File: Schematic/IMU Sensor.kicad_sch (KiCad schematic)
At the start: 17 parts, among them J31 IMU_nRESET, J32 IMU_INT, U25 BNO086, Y1 32.768k

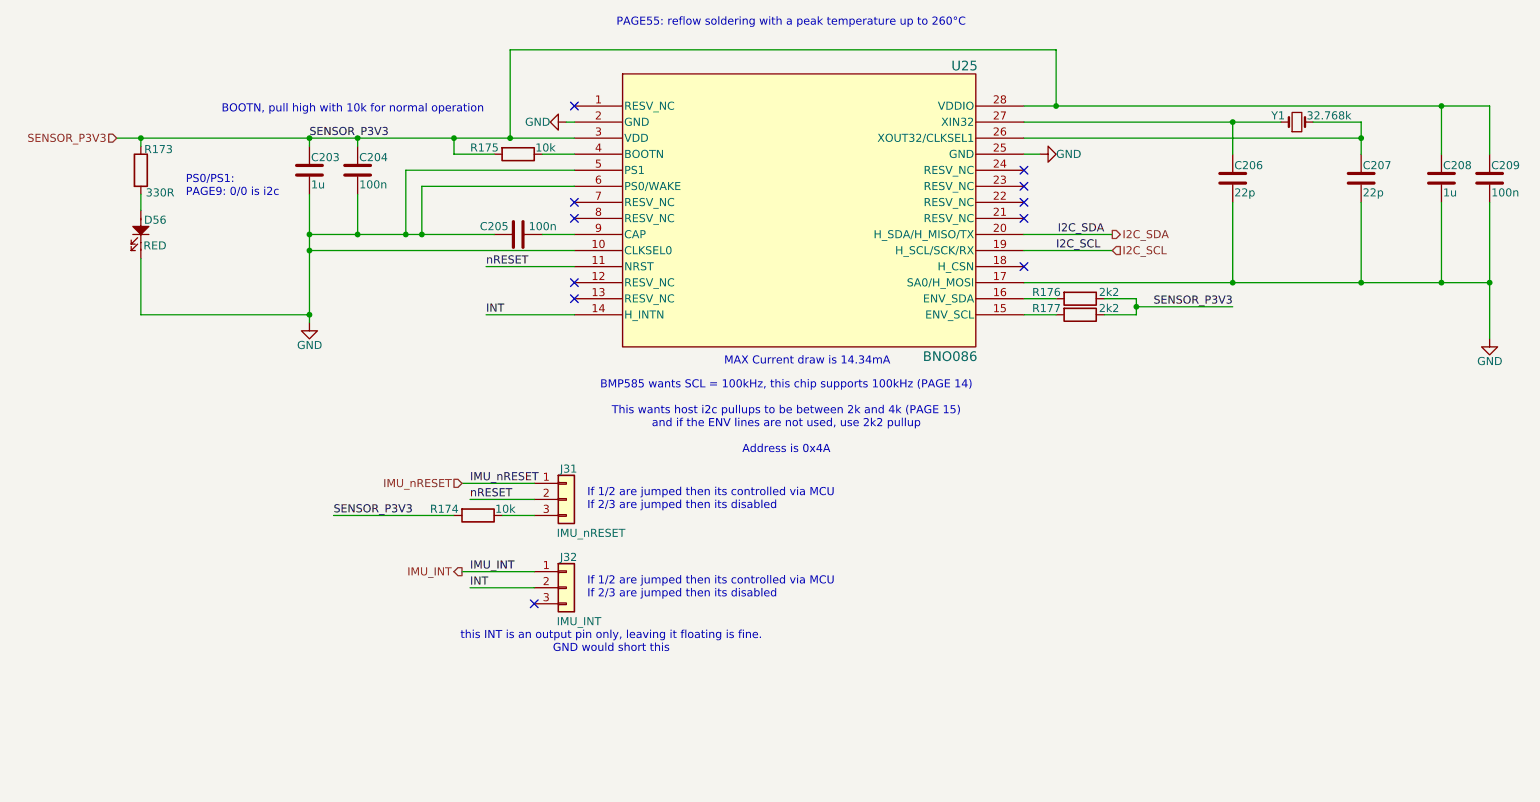
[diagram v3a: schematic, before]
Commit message: updated fuel guage
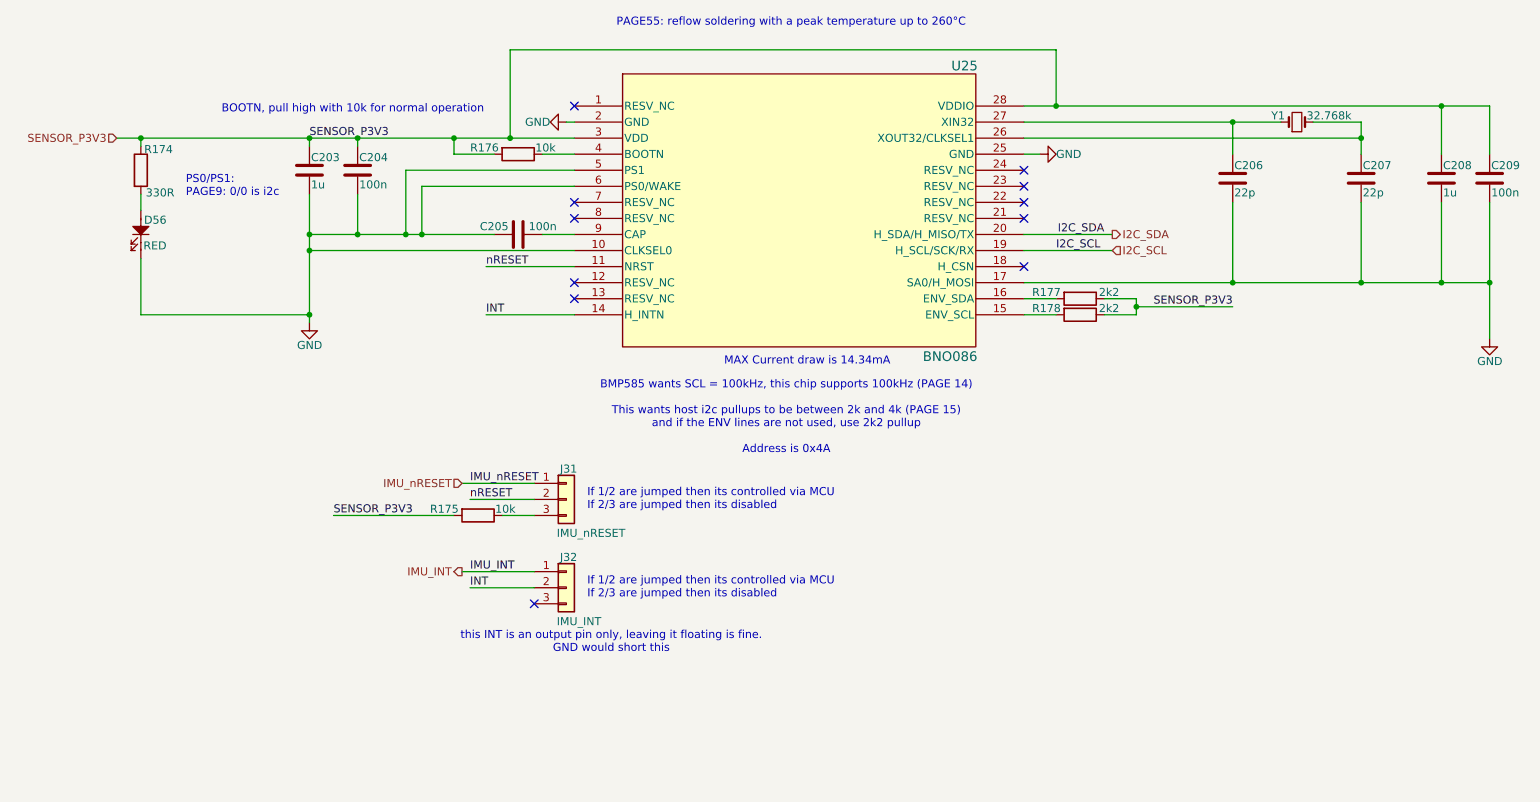
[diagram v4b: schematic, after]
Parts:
- renumbered R173 to R174, R174 to R175, R175 to R176, R176 to R177, R177 to R178
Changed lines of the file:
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@@
 		(on_board yes)
 		(dnp no)
-		(property "Reference" "R175"
+		(property "Reference" "R176"
 			(at 100.076 87.884 90)
 			(effects
@@
 			(project "STAR"
 				(path "/fc8533bc-25dd-4c20-9b4c-ffebebd6739b/93231d0a-659f-4d39-8e8d-78b96a3896a1/75e06a36-2807-4a4b-af1f-d37310ed1ba6"
-					(reference "R175")
+					(reference "R176")
 					(unit 1)
 				)
@@
 		(on_board yes)
 		(dnp no)
-		(property "Reference" "R177"
+		(property "Reference" "R178"
 			(at 188.976 113.284 90)
 			(effects
@@
 			(project "STAR"
 				(path "/fc8533bc-25dd-4c20-9b4c-ffebebd6739b/93231d0a-659f-4d39-8e8d-78b96a3896a1/75e06a36-2807-4a4b-af1f-d37310ed1ba6"
-					(reference "R177")
+					(reference "R178")
 					(unit 1)
 				)
@@
 		(on_board yes)
 		(dnp no)
-		(property "Reference" "R173"
+		(property "Reference" "R174"
 			(at 48.514 88.138 0)
 			(effects
@@
 			(project "STAR"
 				(path "/fc8533bc-25dd-4c20-9b4c-ffebebd6739b/93231d0a-659f-4d39-8e8d-78b96a3896a1/75e06a36-2807-4a4b-af1f-d37310ed1ba6"
-					(reference "R173")
+					(reference "R174")
 					(unit 1)
 				)
@@
 		(on_board yes)
 		(dnp no)
-		(property "Reference" "R176"
+		(property "Reference" "R177"
 			(at 188.976 110.744 90)
 			(effects
@@
 			(project "STAR"
 				(path "/fc8533bc-25dd-4c20-9b4c-ffebebd6739b/93231d0a-659f-4d39-8e8d-78b96a3896a1/75e06a36-2807-4a4b-af1f-d37310ed1ba6"
-					(reference "R176")
+					(reference "R177")
 					(unit 1)
 				)
@@
 		(on_board yes)
 		(dnp no)
-		(property "Reference" "R174"
+		(property "Reference" "R175"
 			(at 93.726 145.034 90)
 			(effects
@@
 			(project "STAR"
 				(path "/fc8533bc-25dd-4c20-9b4c-ffebebd6739b/93231d0a-659f-4d39-8e8d-78b96a3896a1/75e06a36-2807-4a4b-af1f-d37310ed1ba6"
-					(reference "R174")
+					(reference "R175")
 					(unit 1)
 				)

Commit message: Added MCU
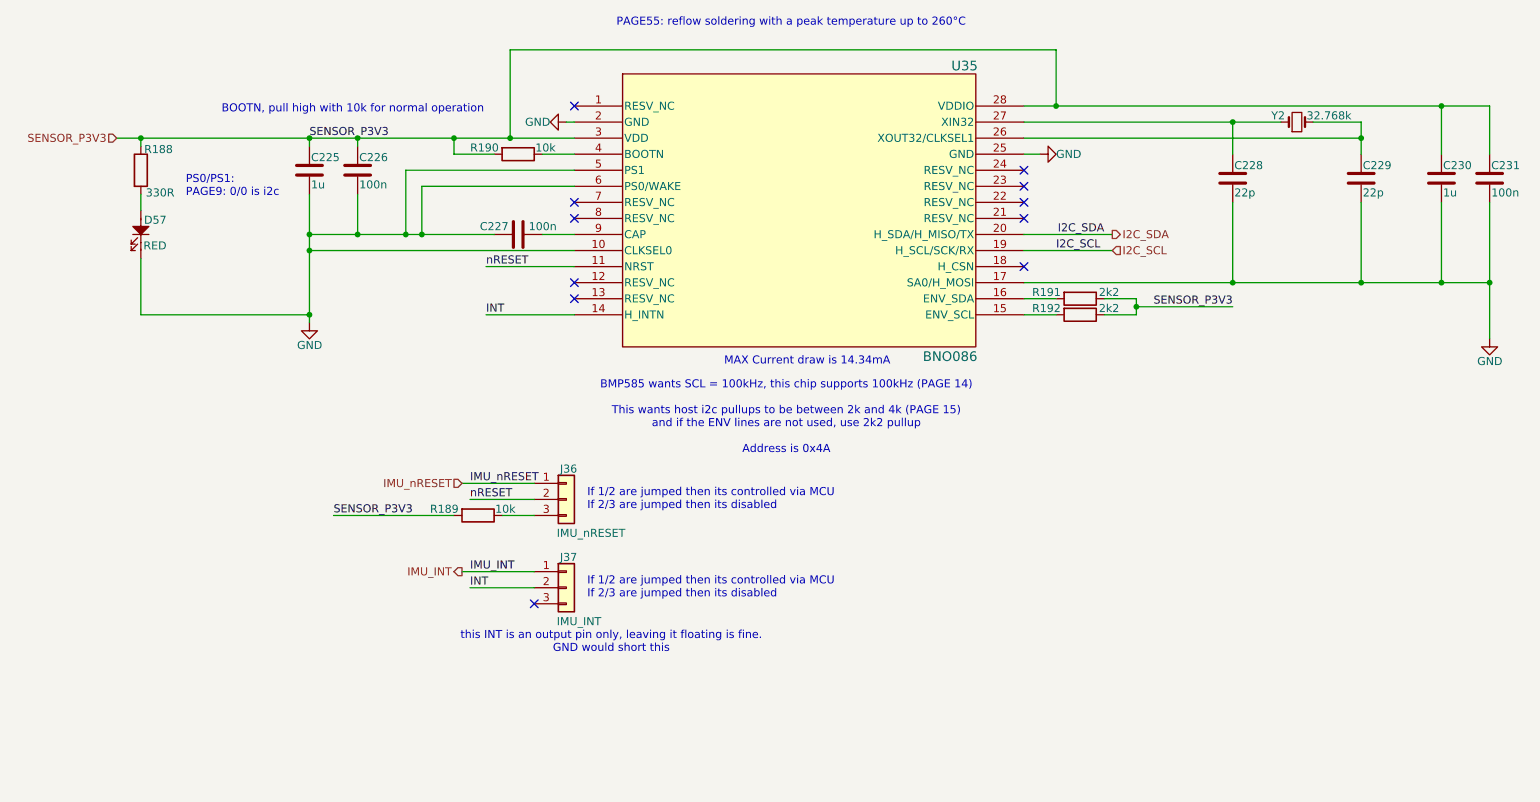
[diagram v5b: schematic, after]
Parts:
- renumbered C203 to C225, C204 to C226, C205 to C227, C206 to C228, C207 to C229, C208 to C230, C209 to C231, D56 to D57, J31 to J36, J32 to J37, R174 to R188, R175 to R189, R176 to R190, R177 to R191, R178 to R192, U25 to U35, Y1 to Y2
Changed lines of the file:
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@@
 		(on_board yes)
 		(dnp no)
-		(property "Reference" "R176"
+		(property "Reference" "R190"
 			(at 100.076 87.884 90)
 			(effects
@@
 			(project "STAR"
 				(path "/fc8533bc-25dd-4c20-9b4c-ffebebd6739b/93231d0a-659f-4d39-8e8d-78b96a3896a1/75e06a36-2807-4a4b-af1f-d37310ed1ba6"
-					(reference "R176")
+					(reference "R190")
 					(unit 1)
 				)
@@
 		(on_board yes)
 		(dnp no)
-		(property "Reference" "R178"
+		(property "Reference" "R192"
 			(at 188.976 113.284 90)
 			(effects
@@
 			(project "STAR"
 				(path "/fc8533bc-25dd-4c20-9b4c-ffebebd6739b/93231d0a-659f-4d39-8e8d-78b96a3896a1/75e06a36-2807-4a4b-af1f-d37310ed1ba6"
-					(reference "R178")
+					(reference "R192")
 					(unit 1)
 				)
@@
 		(on_board yes)
 		(dnp no)
-		(property "Reference" "#PWR0113"
+		(property "Reference" "#PWR0125"
 			(at 194.31 88.9 0)
 			(effects
@@
 			(project "STAR"
 				(path "/fc8533bc-25dd-4c20-9b4c-ffebebd6739b/93231d0a-659f-4d39-8e8d-78b96a3896a1/75e06a36-2807-4a4b-af1f-d37310ed1ba6"
-					(reference "#PWR0113")
+					(reference "#PWR0125")
 					(unit 1)
 				)
@@
 		(on_board yes)
 		(dnp no)
-		(property "Reference" "U25"
+		(property "Reference" "U35"
 			(at 176.022 74.93 0)
 			(effects
@@
 			(project ""
 				(path "/fc8533bc-25dd-4c20-9b4c-ffebebd6739b/93231d0a-659f-4d39-8e8d-78b96a3896a1/75e06a36-2807-4a4b-af1f-d37310ed1ba6"
-					(reference "U25")
+					(reference "U35")
 					(unit 1)
 				)
@@
 		(on_board yes)
 		(dnp no)
-		(property "Reference" "C208"
+		(property "Reference" "C230"
 			(at 251.714 90.678 0)
 			(effects
@@
 			(project "STAR"
 				(path "/fc8533bc-25dd-4c20-9b4c-ffebebd6739b/93231d0a-659f-4d39-8e8d-78b96a3896a1/75e06a36-2807-4a4b-af1f-d37310ed1ba6"
-					(reference "C208")
+					(reference "C230")
 					(unit 1)
 				)
@@
 		(on_board yes)
 		(dnp no)
-		(property "Reference" "C205"
+		(property "Reference" "C227"
 			(at 103.886 100.33 90)
 			(effects
@@
 			(project "STAR"
 				(path "/fc8533bc-25dd-4c20-9b4c-ffebebd6739b/93231d0a-659f-4d39-8e8d-78b96a3896a1/75e06a36-2807-4a4b-af1f-d37310ed1ba6"
-					(reference "C205")
+					(reference "C227")
 					(unit 1)
 				)
@@
 		(on_board yes)
 		(dnp no)
-		(property "Reference" "R174"
+		(property "Reference" "R188"
 			(at 48.514 88.138 0)
 			(effects
@@
 			(project "STAR"
 				(path "/fc8533bc-25dd-4c20-9b4c-ffebebd6739b/93231d0a-659f-4d39-8e8d-78b96a3896a1/75e06a36-2807-4a4b-af1f-d37310ed1ba6"
-					(reference "R174")
+					(reference "R188")
 					(unit 1)
 				)
@@
 		(on_board yes)
 		(dnp no)
-		(property "Reference" "D56"
+		(property "Reference" "D57"
 			(at 49.784 99.314 90)
 			(effects
@@
 			(project "STAR"
 				(path "/fc8533bc-25dd-4c20-9b4c-ffebebd6739b/93231d0a-659f-4d39-8e8d-78b96a3896a1/75e06a36-2807-4a4b-af1f-d37310ed1ba6"
-					(reference "D56")
+					(reference "D57")
 					(unit 1)
 				)
@@
 		(on_board yes)
 		(dnp no)
-		(property "Reference" "#PWR0112"
+		(property "Reference" "#PWR0124"
 			(at 106.68 83.82 0)
 			(effects
@@
 			(project "STAR"
 				(path "/fc8533bc-25dd-4c20-9b4c-ffebebd6739b/93231d0a-659f-4d39-8e8d-78b96a3896a1/75e06a36-2807-4a4b-af1f-d37310ed1ba6"
-					(reference "#PWR0112")
+					(reference "#PWR0124")
 					(unit 1)
 				)
@@
 		(on_board yes)
 		(dnp no)
-		(property "Reference" "J31"
+		(property "Reference" "J36"
 			(at 112.014 138.684 0)
 			(effects
@@
 			(project "STAR"
 				(path "/fc8533bc-25dd-4c20-9b4c-ffebebd6739b/93231d0a-659f-4d39-8e8d-78b96a3896a1/75e06a36-2807-4a4b-af1f-d37310ed1ba6"
-					(reference "J31")
+					(reference "J36")
 					(unit 1)
 				)
@@
 		(on_board yes)
 		(dnp no)
-		(property "Reference" "C204"
+		(property "Reference" "C226"
 			(at 80.264 89.408 0)
 			(effects
@@
 			(project "STAR"
 				(path "/fc8533bc-25dd-4c20-9b4c-ffebebd6739b/93231d0a-659f-4d39-8e8d-78b96a3896a1/75e06a36-2807-4a4b-af1f-d37310ed1ba6"
-					(reference "C204")
+					(reference "C226")
 					(unit 1)
 				)
@@
 		(on_board yes)
 		(dnp no)
-		(property "Reference" "J32"
+		(property "Reference" "J37"
 			(at 112.014 152.654 0)
 			(effects
@@
 			(project "STAR"
 				(path "/fc8533bc-25dd-4c20-9b4c-ffebebd6739b/93231d0a-659f-4d39-8e8d-78b96a3896a1/75e06a36-2807-4a4b-af1f-d37310ed1ba6"
-					(reference "J32")
+					(reference "J37")
 					(unit 1)
 				)
@@
 		(on_board yes)
 		(dnp no)
-		(property "Reference" "R177"
+		(property "Reference" "R191"
 			(at 188.976 110.744 90)
 			(effects
@@
 			(project "STAR"
 				(path "/fc8533bc-25dd-4c20-9b4c-ffebebd6739b/93231d0a-659f-4d39-8e8d-78b96a3896a1/75e06a36-2807-4a4b-af1f-d37310ed1ba6"
-					(reference "R177")
+					(reference "R191")
 					(unit 1)
 				)
@@
 		(on_board yes)
 		(dnp no)
-		(property "Reference" "C206"
+		(property "Reference" "C228"
 			(at 218.694 90.678 0)
 			(effects
@@
 			(project "STAR"
 				(path "/fc8533bc-25dd-4c20-9b4c-ffebebd6739b/93231d0a-659f-4d39-8e8d-78b96a3896a1/75e06a36-2807-4a4b-af1f-d37310ed1ba6"
-					(reference "C206")
+					(reference "C228")
 					(unit 1)
 				)
@@
 		(on_board yes)
 		(dnp no)
-		(property "Reference" "#PWR0111"
+		(property "Reference" "#PWR0123"
 			(at 72.39 121.92 0)
 			(effects
@@
 			(project "STAR"
 				(path "/fc8533bc-25dd-4c20-9b4c-ffebebd6739b/93231d0a-659f-4d39-8e8d-78b96a3896a1/75e06a36-2807-4a4b-af1f-d37310ed1ba6"
-					(reference "#PWR0111")
+					(reference "#PWR0123")
 					(unit 1)
 				)
@@
 		(on_board yes)
 		(dnp no)
-		(property "Reference" "C207"
+		(property "Reference" "C229"
 			(at 239.014 90.678 0)
 			(effects
@@
 			(project "STAR"
 				(path "/fc8533bc-25dd-4c20-9b4c-ffebebd6739b/93231d0a-659f-4d39-8e8d-78b96a3896a1/75e06a36-2807-4a4b-af1f-d37310ed1ba6"
-					(reference "C207")
+					(reference "C229")
 					(unit 1)
 				)
@@
 		(on_board yes)
 		(dnp no)
-		(property "Reference" "R175"
+		(property "Reference" "R189"
 			(at 93.726 145.034 90)
 			(effects
@@
 			(project "STAR"
 				(path "/fc8533bc-25dd-4c20-9b4c-ffebebd6739b/93231d0a-659f-4d39-8e8d-78b96a3896a1/75e06a36-2807-4a4b-af1f-d37310ed1ba6"
-					(reference "R175")
+					(reference "R189")
 					(unit 1)
 				)
@@
 		(on_board yes)
 		(dnp no)
-		(property "Reference" "C209"
+		(property "Reference" "C231"
 			(at 259.334 90.678 0)
 			(effects
@@
 			(project "STAR"
 				(path "/fc8533bc-25dd-4c20-9b4c-ffebebd6739b/93231d0a-659f-4d39-8e8d-78b96a3896a1/75e06a36-2807-4a4b-af1f-d37310ed1ba6"
-					(reference "C209")
+					(reference "C231")
 					(unit 1)
 				)
@@
 		(on_board yes)
 		(dnp no)
-		(property "Reference" "#PWR0114"
+		(property "Reference" "#PWR0126"
 			(at 259.08 124.46 0)
 			(effects
@@
 			(project "STAR"
 				(path "/fc8533bc-25dd-4c20-9b4c-ffebebd6739b/93231d0a-659f-4d39-8e8d-78b96a3896a1/75e06a36-2807-4a4b-af1f-d37310ed1ba6"
-					(reference "#PWR0114")
+					(reference "#PWR0126")
 					(unit 1)
 				)
@@
 		(on_board yes)
 		(dnp no)
-		(property "Reference" "C203"
+		(property "Reference" "C225"
 			(at 72.644 89.408 0)
 			(effects
@@
 			(project "STAR"
 				(path "/fc8533bc-25dd-4c20-9b4c-ffebebd6739b/93231d0a-659f-4d39-8e8d-78b96a3896a1/75e06a36-2807-4a4b-af1f-d37310ed1ba6"
-					(reference "C203")
+					(reference "C225")
 					(unit 1)
 				)
@@
 		(on_board yes)
 		(dnp no)
-		(property "Reference" "Y1"
+		(property "Reference" "Y2"
 			(at 224.536 82.804 0)
 			(effects
@@
 			(project ""
 				(path "/fc8533bc-25dd-4c20-9b4c-ffebebd6739b/93231d0a-659f-4d39-8e8d-78b96a3896a1/75e06a36-2807-4a4b-af1f-d37310ed1ba6"
-					(reference "Y1")
+					(reference "Y2")
 					(unit 1)
 				)

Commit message: Started to work on the BOM
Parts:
- added TP171, TP172: TestPoint, symbol Connector:TestPoint
- C221: renamed from C225; footprint (none) -> Capacitor_SMD:C_1206_3216Metric_Pad1.33x1.80mm_HandSolder; Link (none) -> https://mou.sr/41y0aEA; Manufacturer Part Number (none) -> CL31B105KBHNNNE; Price per Unit (none) -> 0.11; Supplier (none) -> Mouser; Supplier Part Number (none) -> 187-CL31B105KBHNNNE; now not fitted; now left out of the parts list
- C222: renamed from C226; footprint (none) -> Capacitor_SMD:C_1206_3216Metric_Pad1.33x1.80mm_HandSolder; Link (none) -> https://mou.sr/4n9ybmQ; Manufacturer Part Number (none) -> CL31B104KBCNNNC; Price per Unit (none) -> 0.11; Supplier (none) -> Mouser; Supplier Part Number (none) -> 187-CL31B104KBCNNNC; now not fitted; now left out of the parts list
- C223: renamed from C227; footprint (none) -> Capacitor_SMD:C_1206_3216Metric_Pad1.33x1.80mm_HandSolder; Link (none) -> https://mou.sr/4n9ybmQ; Manufacturer Part Number (none) -> CL31B104KBCNNNC; Price per Unit (none) -> 0.11; Supplier (none) -> Mouser; Supplier Part Number (none) -> 187-CL31B104KBCNNNC; now not fitted; now left out of the parts list
- C224: renamed from C228; footprint (none) -> Capacitor_SMD:C_0603_1608Metric_Pad1.08x0.95mm_HandSolder; Link (none) -> https://mou.sr/3JpGcTh; Manufacturer Part Number (none) -> CL10C220JB8NNNC; Price per Unit (none) -> 0.10; Supplier (none) -> Mouser; Supplier Part Number (none) -> 187-CL10C220JB8NNNC; now not fitted; now left out of the parts list
- C225: renamed from C229; footprint (none) -> Capacitor_SMD:C_0603_1608Metric_Pad1.08x0.95mm_HandSolder; Link (none) -> https://mou.sr/3JpGcTh; Manufacturer Part Number (none) -> CL10C220JB8NNNC; Price per Unit (none) -> 0.10; Supplier (none) -> Mouser; Supplier Part Number (none) -> 187-CL10C220JB8NNNC; now not fitted; now left out of the parts list
- C226: renamed from C230; footprint (none) -> Capacitor_SMD:C_1206_3216Metric_Pad1.33x1.80mm_HandSolder; Link (none) -> https://mou.sr/41y0aEA; Manufacturer Part Number (none) -> CL31B105KBHNNNE; Price per Unit (none) -> 0.11; Supplier (none) -> Mouser; Supplier Part Number (none) -> 187-CL31B105KBHNNNE; now not fitted; now left out of the parts list
- C227: renamed from C231; footprint (none) -> Capacitor_SMD:C_1206_3216Metric_Pad1.33x1.80mm_HandSolder; Link (none) -> https://mou.sr/4n9ybmQ; Manufacturer Part Number (none) -> CL31B104KBCNNNC; Price per Unit (none) -> 0.11; Supplier (none) -> Mouser; Supplier Part Number (none) -> 187-CL31B104KBCNNNC; now not fitted; now left out of the parts list
- D54: renamed from D57; footprint PCM_Diode_SMD_AKL:D_0805_2012Metric -> ASMM-CR03-BU802:LEDM3528X210N; Link (none) -> https://mou.sr/460BFB7; Manufacturer Part Number (none) -> ASMM-CR03-BU802; Price per Unit (none) -> 0.32; Supplier (none) -> Mouser; Supplier Part Number (none) -> 630-ASMM-CR03-BU802; now not fitted; now left out of the parts list
- J34: renamed from J36; now not fitted; now left out of the parts list
- J35: renamed from J37; now not fitted; now left out of the parts list
- R184: renamed from R188; now not fitted; now left out of the parts list
- R185: renamed from R189; now not fitted; now left out of the parts list
- R186: renamed from R190; now not fitted; now left out of the parts list
- R187: renamed from R191; now not fitted; now left out of the parts list
- R188: renamed from R192; now not fitted; now left out of the parts list
- U33: renamed from U35; footprint QFN28_BNO086_CEV -> (none); now not fitted; now left out of the parts list
- Y2: now not fitted; now left out of the parts list
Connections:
- net IMU_INT: now also TP172.1
- net IMU_nRESET: now also TP171.1
